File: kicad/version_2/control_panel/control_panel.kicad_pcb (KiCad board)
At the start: 2 copper layers, 161.9 x 75.6 mm, 41 parts, among them J1 Conn_01x01_Pin, J2 Conn_01x01_Pin, J3 Conn_01x01_Pin, J4 Conn_01x01_Pin, SW1 SW_Push

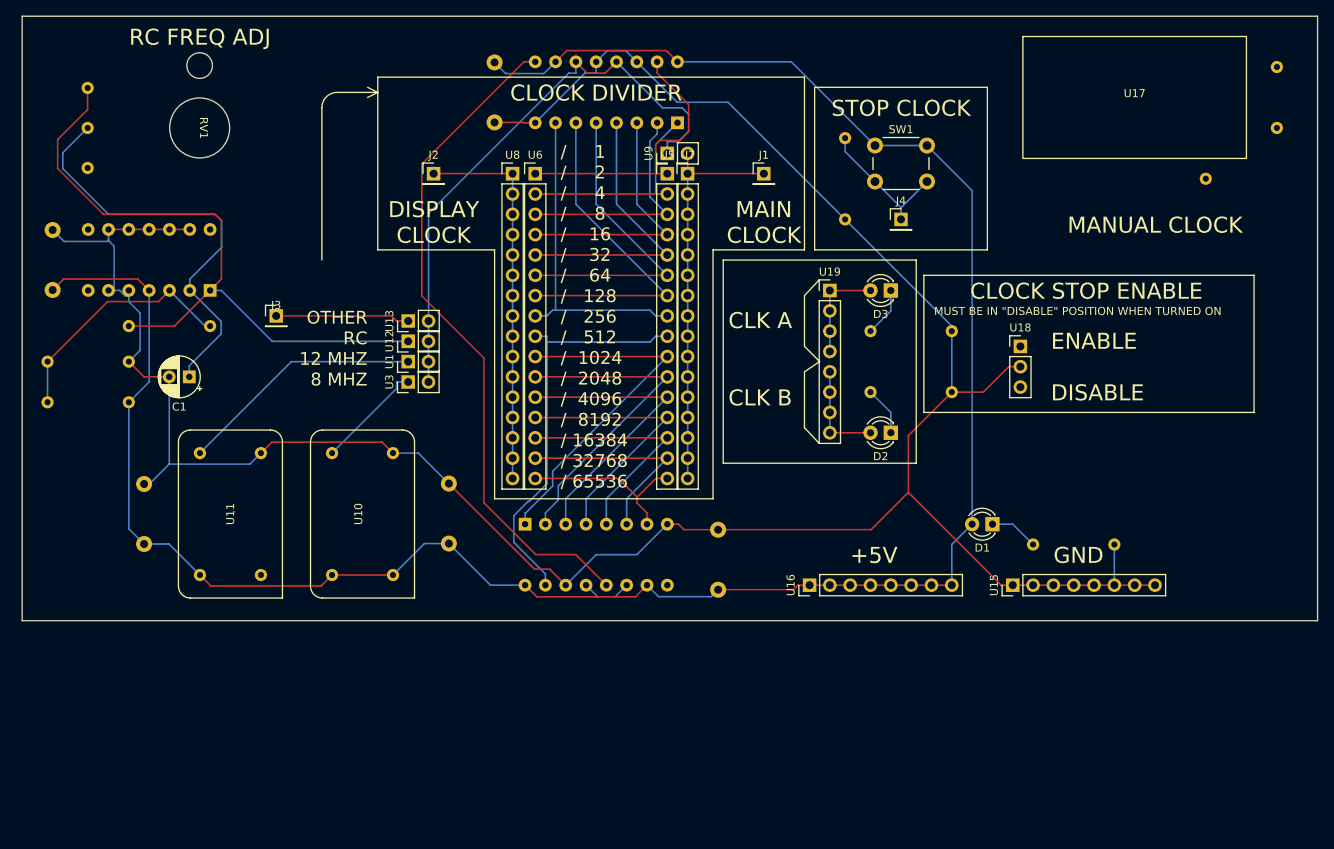
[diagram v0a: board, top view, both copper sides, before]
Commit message: Improved control panel and fixed music program
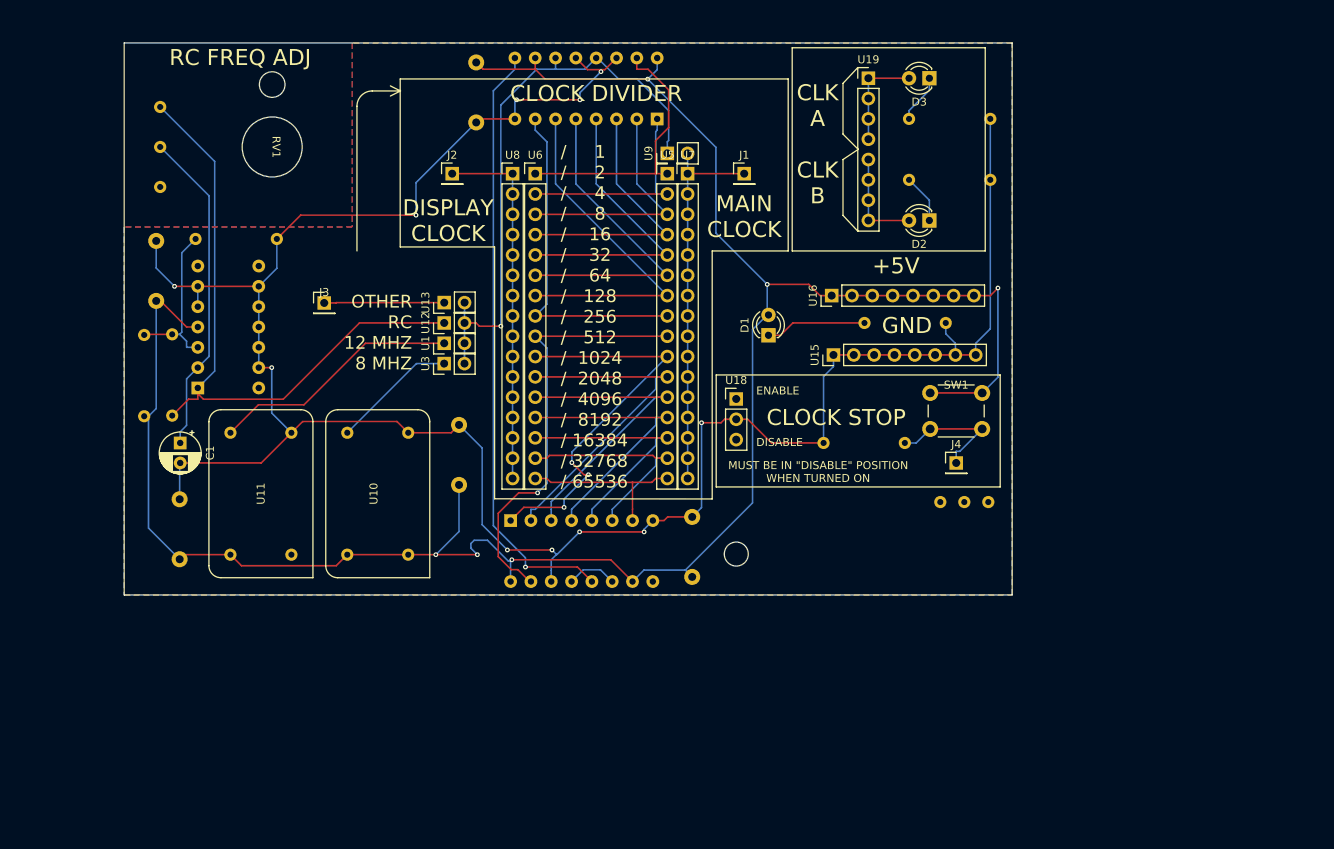
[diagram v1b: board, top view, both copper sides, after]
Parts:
- U17: footprint custom_footprint_library:manual_clock_switch -> custom_footprint_library:manual_clock_switch_side; moved to B.Cu
- moved U17 73.4 mm to (156.0, 106.4)
- moved D1 36.6 mm to (148.5, 73.5), turned to 90 degrees
- moved U15 36.5 mm to (156.7, 76.0)
- moved U16 36.3 mm to (156.4, 68.6)
- moved U18 36.1 mm to (144.5, 81.5)
- moved R4 34.8 mm to (165.6, 72.0)
- moved R1 33.1 mm to (160.5, 87.0), turned to 90 degrees
- moved SW1 31.7 mm to (168.8, 80.8)
- moved J4 31.2 mm to (172.0, 89.5)
- moved R7 27.0 mm to (171.2, 46.5)
- moved D2 27.0 mm to (168.6, 59.2)
- moved D3 27.0 mm to (168.6, 41.4)
- moved R6 27.0 mm to (171.2, 54.1)
- moved U19 27.0 mm to (161.0, 41.4)
- moved R2 24.0 mm to (82.0, 61.5)
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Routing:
- net Net-(U10-GND): track 315.4 -> 290.2 mm, vias 0 -> 11
- net Net-(U14-IN-_1): track 53.4 -> 41.0 mm
- net Net-(U14-IN+_1): track 30.9 -> 20.6 mm
- net Net-(U2-RCO#): track 84.6 -> 75.5 mm, vias 0 -> 1
- net Net-(D1-K): track 6.13 -> 12.6 mm
- net Net-(U4-Q1): track 44.9 -> 50.1 mm, vias 0 -> 3
- net Net-(U12-A): track 83.5 -> 79.3 mm
- net Net-(U4-Q0): track 51.3 -> 54.0 mm, vias 0 -> 1
- net Net-(J1-Pin_1): track 50.2 -> 47.7 mm
- net Net-(J2-Pin_1): track 48.0 -> 45.6 mm
- net Net-(U10-CLK): track 13.7 -> 15.7 mm
- net Net-(U2-Q7): track 40.5 -> 42.3 mm
- net Net-(J3-Pin_1): track 16.8 -> 15.0 mm
- net Net-(U2-Q5): track 39.3 -> 40.8 mm
- net Net-(U2-Q3): track 32.1 -> 33.6 mm
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- added copper zone on F.Cu, net Net-(D1-A)
- added copper zone on B.Cu, net Net-(U10-GND)
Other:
- board size 161.9 x 75.6 mm -> 111 x 69 mm
- board text added: "CLOCK STOP"
- board text removed: "CLOCK STOP ENABLE"
- board text removed: "MANUAL CLOCK"
- board text removed: "STOP CLOCK"

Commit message: Finished control panel
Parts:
- added R10: R, custom_footprint_library:0.4_pitch_resistor, B.Cu at (62.0, 82.0)
- added R11: R, custom_footprint_library:0.4_pitch_resistor, B.Cu at (62.0, 95.5)
- added R12: R, custom_footprint_library:0.4_pitch_resistor, B.Cu at (62.0, 109.0)
- added R13: R, custom_footprint_library:0.4_pitch_resistor, B.Cu at (62.0, 122.5)
- added R8: R, custom_footprint_library:0.4_pitch_resistor, B.Cu at (62.0, 55.0)
- added R9: R, custom_footprint_library:0.4_pitch_resistor, B.Cu at (62.0, 68.5)
- added SW2: SW_Push, Button_Switch_THT:SW_PUSH_6mm, F.Cu at (58.8, 52.8)
- added SW3: SW_Push, Button_Switch_THT:SW_PUSH_6mm, F.Cu at (58.8, 66.2)
- added SW4: SW_Push, Button_Switch_THT:SW_PUSH_6mm, F.Cu at (58.8, 79.8)
- added SW5: SW_Push, Button_Switch_THT:SW_PUSH_6mm, F.Cu at (58.8, 93.2)
- added SW6: SW_Push, Button_Switch_THT:SW_PUSH_6mm, F.Cu at (58.8, 106.8)
- added SW7: SW_Push, Button_Switch_THT:SW_PUSH_6mm, F.Cu at (58.8, 120.2)
- added U20: ~, Connector_PinHeader_2.54mm:PinHeader_1x08_P2.54mm_Vertical, F.Cu at (72.4, 57.5)
- added U21: ~, Connector_PinHeader_2.54mm:PinHeader_1x10_P2.54mm_Horizontal, F.Cu at (172.9, 125.6)
- added U22: ~, Connector_PinHeader_2.54mm:PinHeader_1x08_P2.54mm_Vertical, F.Cu at (113.0, 57.5)
- C2, C3, C4, C5, C6: footprint Capacitor_THT:C_Rect_L10.3mm_W4.5mm_P7.50mm_MKS4 -> Capacitor_THT:C_Rect_L11.0mm_W4.2mm_P10.00mm_MKT
- U17: moved to F.Cu
- moved U17 59.3 mm to (153.5, 47.1)
- moved C3 25.5 mm to (75.5, 127.0)
- moved C6 25.3 mm to (73.0, 94.5)
- moved C5 24.3 mm to (140.0, 128.0)
- moved U2 24.1 mm to (135.2, 70.6)
- moved R5 24.0 mm to (75.4, 102.5)
- moved C1 24.0 mm to (76.0, 111.0)
- moved R3 23.9 mm to (71.5, 102.5)
- moved U10 23.5 mm to (101.1, 116.8)
- moved U13 23.5 mm to (109.4, 92.9)
- moved U16 23.5 mm to (157.8, 92.0)
- moved U9 23.5 mm to (137.3, 74.3)
- moved D2 23.5 mm to (170.0, 82.7)
- moved D3 23.5 mm to (170.0, 64.9)
- moved R7 23.5 mm to (172.6, 70.0)
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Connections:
- U4 pad 11: Net-(U4-CCLK) -> Net-(U1-B)
- U4 pad 13: Net-(U4-CCLK) -> Net-(U1-B)
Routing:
- net Net-(D1-A): track 274.3 -> 379.4 mm, vias 6 -> 5
- net Net-(U20-5): track 0.00 -> 91.3 mm
- net Net-(U10-GND): track 290.2 -> 373.9 mm
- net Net-(U20-4): track 0.00 -> 66.5 mm
- net Net-(U20-3): track 0.00 -> 52.8 mm
- net Net-(U1-B): track 72.9 -> 111.3 mm, vias 1 -> 0
- net Net-(U20-2): track 0.00 -> 38.2 mm
- net Net-(U20-1): track 0.00 -> 25.3 mm
- net Net-(U20-0): track 0.00 -> 18.0 mm
- net Net-(U2-Q0): track 34.1 -> 46.3 mm
- net Net-(U4-Q0): track 54.0 -> 63.5 mm
- net Net-(U4-Q1): track 50.1 -> 42.1 mm, vias 3 -> 1
- net Net-(U4-CCLK): track 6.29 -> 0.00 mm
- net Net-(U4-Q2): track 42.7 -> 36.5 mm
- net Net-(U2-Q6): track 44.4 -> 38.6 mm
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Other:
- board size 111 x 69 mm -> 126.5 x 84 mm
- board text added: "0 ........................................... 9"
- board text added: "0 1 2 3 4 5"
- board text added: "INPUTS 0 ........ 5 <- BUTTONS"
- board text added: "OUTPUTS"

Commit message: before using copilot
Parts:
- SW2, SW3, SW4, SW5, SW6, SW7: footprint Button_Switch_THT:SW_PUSH_6mm -> custom_footprint_library:2_pin_button
- moved C1 6.14 mm to (70.0, 112.3)
- moved R3 2.55 mm to (69.0, 103.0)
- moved R5 1.93 mm to (73.5, 103.0)
- moved U4 1.83 mm to (118.1, 120.2)
- moved U2 1.50 mm to (133.7, 70.5)
- moved C6 0.50 mm to (73.5, 94.5)
- moved U8 0.19 mm to (118.1, 76.8)
- moved U6 0.09 mm to (120.7, 76.8)
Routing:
- net Net-(D1-A): track 379.4 -> 350.5 mm, vias 5 -> 10
- net Net-(U1-B): track 111.3 -> 127.0 mm, vias 0 -> 1
- net Net-(U20-5): track 91.3 -> 77.5 mm
- net Net-(U2-Q0): track 46.3 -> 33.9 mm
- net Net-(U10-GND): track 373.9 -> 363.9 mm, vias 11 -> 10
- net Net-(U4-Q0): track 63.5 -> 73.0 mm, vias 1 -> 2
- net Net-(U20-2): track 38.2 -> 32.6 mm
- net Net-(U20-3): track 52.8 -> 47.5 mm
- net Net-(U4-Q3): track 34.0 -> 39.0 mm, vias 1 -> 0
- net Net-(U4-Q4): track 30.6 -> 35.0 mm, vias 1 -> 0
- net Net-(U20-4): track 66.5 -> 62.1 mm
- net Net-(U14-IN-_1): track 41.7 -> 46.1 mm
- net Net-(U14-IN+_1): track 21.2 -> 24.7 mm
- net Net-(U20-0): track 18.0 -> 21.3 mm
- net Net-(U2-Q7): track 44.0 -> 47.0 mm
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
